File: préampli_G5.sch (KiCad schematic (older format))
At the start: 44 parts, among them J1 Input, J2 Barrel_Jack, J3 Output, SW1 Boost, U1 ECC83, U2 ECC83, U3 NCH6100HV

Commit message: Use a self-split PP for the output stage
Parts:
- removed C10: 10µF, symbol Device:CP
- removed C8: 470pF, symbol Device:C
- removed R13: 470k, symbol Device:R
- removed R15: 100k, symbol Device:R
- removed R17: 10k, symbol Device:R
- added R6: 220k, symbol Device:R
- added TR1: HAMMOND 125A, symbol Transformer:TRANSF4
- R14: value 1.8k -> 1k
- R16: value 91k -> 180R/2W
- U3: symbol Converter_DCDC:NCH6100HV -> préampli_G5-rescue:NCH6100HV-Converter_DCDC
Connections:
- net GND: now also R16.2, SW1.4, U2.7 (G), TR1.4
- net GNDPWR: now also U3.2 (SHDN)
- net at C6.1, R20.1, R8.1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: no longer SW1.3
- net at R11.2, R12.1, R19.1: now also R6.1
- net at U2.1 (A): now also TR1.1; no longer U2.7 (G)
- net at U2.2 (G): now also R6.2
- net at R14.1, U2.3 (K): now also U2.8 (K)
- net at C9.1, R10.1, R18.2: now also TR1.2; no longer U2.6 (A)
- net at R16.1: now also RV6.3, TR1.5; no longer U2.8 (K)
- net at R19.2: now also SW1.3; no longer SW1.4
- new net: TR1.3, U2.6 (A)
- no-connect marks 1 -> 0
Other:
- note added: "NOTE: TR1 OUPUT ON PINS 3 & 5\nVOLTAGE RATIO 46.9:1 (-33.4 dB)\nIMPEDANCE RATIO 2200:1\nPRIMARY IMPEDANCE 336kΩ (168kΩ PER ANODE)"
- moved on the sheet: C11, J3, R14, R19, R20, RV6, SW1

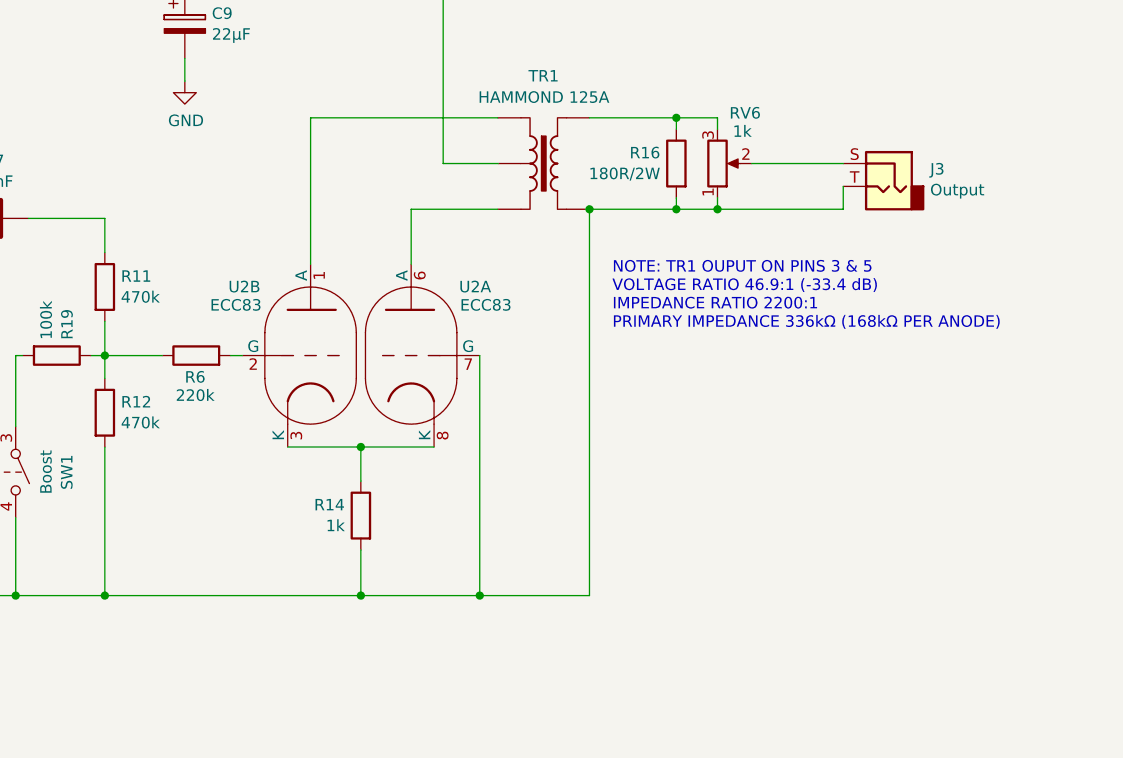
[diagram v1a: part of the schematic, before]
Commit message: Switch to LTP & fix transformer load
180R value for R16 wasn't appropriate, as we should aim for a 100k anode
load for the output stage. Replacing it with 100R will give us the right
primary impedance.

Also, the self-split output stage seems to be quite unbalanced,
switching back to an LTP circuit will improve things.
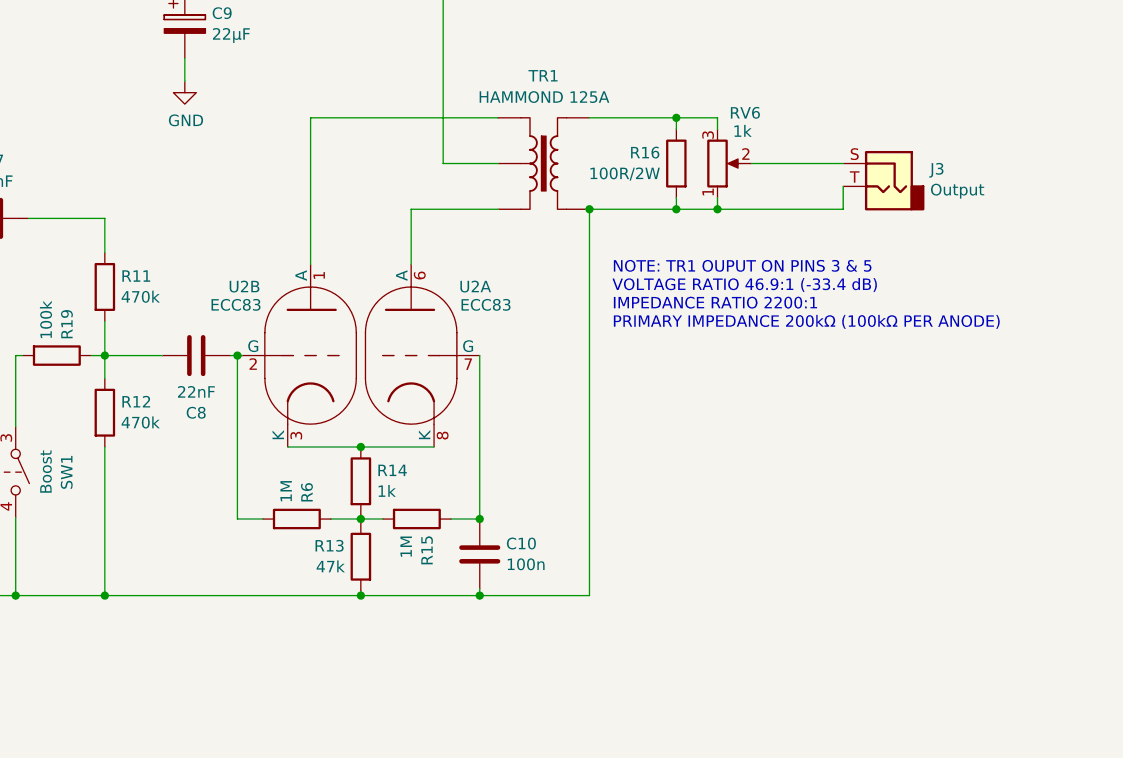
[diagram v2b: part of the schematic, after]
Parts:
- added C10: 100n, symbol Device:C
- added C8: 22nF, symbol Device:C
- added R13: 47k, symbol Device:R
- added R15: 1M, symbol Device:R
- R16: value 180R/2W -> 100R/2W
- R6: value 220k -> 1M
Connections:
- net GND: now also C10.2, R13.2; no longer R14.2, U2.7 (G)
- net at R11.2, R12.1, R19.1: now also C8.2; no longer R6.1
- net at R6.2, U2.2 (G): now also C8.1
- new net: R13.1, R14.2, R15.2, R6.1
- new net: C10.1, R15.1, U2.7 (G)
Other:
- note added: "NOTE: TR1 OUPUT ON PINS 3 & 5\nVOLTAGE RATIO 46.9:1 (-33.4 dB)\nIMPEDANCE RATIO 2200:1\nPRIMARY IMPEDANCE 200kΩ (100kΩ PER ANODE)"
- note removed: "NOTE: TR1 OUPUT ON PINS 3 & 5\nVOLTAGE RATIO 46.9:1 (-33.4 dB)\nIMPEDANCE RATIO 2200:1\nPRIMARY IMPEDANCE 336kΩ (168kΩ PER ANODE)"
- moved on the sheet: R14
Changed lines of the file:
@@
 L Device:R R14
 U 1 1 5C6DBFC3
-P 7820 3800
-F 0 "R14" H 7890 3846 50  0000 L CNN
-F 1 "1k" H 7890 3755 50  0000 L CNN
-F 2 "" V 7750 3800 50  0001 C CNN
-F 3 "~" H 7820 3800 50  0001 C CNN
-	1    7820 3800
-	-1   0    0    -1
+P 7820 3650
+F 0 "R14" H 7890 3696 50  0000 L CNN
+F 1 "1k" H 7890 3605 50  0000 L CNN
+F 2 "" V 7750 3650 50  0001 C CNN
+F 3 "~" H 7820 3650 50  0001 C CNN
+	1    7820 3650
+	1    0    0    -1
 $EndComp
 $Comp
@@
 	6700 2950 6700 3100
 Wire Wire Line
-	7300 3100 7250 3100
+	7300 3100 7280 3100
 Connection ~ 6700 3100
 Wire Wire Line
@@
 P 9200 2260
 F 0 "R16" H 9270 2306 50  0000 L CNN
-F 1 "180R/2W" H 9270 2215 50  0000 L CNN
+F 1 "100R/2W" H 9270 2215 50  0000 L CNN
 F 2 "" V 9130 2260 50  0001 C CNN
 F 3 "~" H 9200 2260 50  0001 C CNN
@@
 	8820 2060 9200 2060
 Text Notes 8920 2990 0    50   ~ 0
-NOTE: TR1 OUPUT ON PINS 3 & 5\nVOLTAGE RATIO 46.9:1 (-33.4 dB)\nIMPEDANCE RATIO 2200:1\nPRIMARY IMPEDANCE 336kΩ (168kΩ PER ANODE)
+NOTE: TR1 OUPUT ON PINS 3 & 5\nVOLTAGE RATIO 46.9:1 (-33.4 dB)\nIMPEDANCE RATIO 2200:1\nPRIMARY IMPEDANCE 200kΩ (100kΩ PER ANODE)
 Wire Wire Line
 	8820 4150 8820 2460
 Connection ~ 8820 2460
 Wire Wire Line
+	8340 3100 8340 3815
+Connection ~ 8340 4150
+Wire Wire Line
+	8340 4150 8820 4150
+Wire Wire Line
+	7500 3500 7820 3500
+Wire Wire Line
 	6700 4150 7820 4150
-Wire Wire Line
-	7500 3500 7820 3500
-Wire Wire Line
-	7820 3650 7820 3500
 Connection ~ 7820 3500
 Wire Wire Line
 	7820 3500 8140 3500
-Wire Wire Line
-	7820 3950 7820 4150
-Connection ~ 7820 4150
-Wire Wire Line
-	7820 4150 8340 4150
-Wire Wire Line
-	8340 3100 8340 4150
-Connection ~ 8340 4150
-Wire Wire Line
-	8340 4150 8820 4150
+$Comp
+L Device:R R13
+U 1 1 5C7859F7
+P 7820 3980
+F 0 "R13" H 7890 4026 50  0000 L CNN
+F 1 "47k" H 7890 3935 50  0000 L CNN
+F 2 "" V 7750 3980 50  0001 C CNN
+F 3 "~" H 7820 3980 50  0001 C CNN
+	1    7820 3980
+	-1   0    0    -1
+$EndComp
+$Comp
+L Device:R R15
+U 1 1 5C785AB9
+P 8065 3815
+F 0 "R15" H 8135 3861 50  0000 L CNN
+F 1 "1M" H 8135 3770 50  0000 L CNN
+F 2 "" V 7995 3815 50  0001 C CNN
+F 3 "~" H 8065 3815 50  0001 C CNN
+	1    8065 3815
+	0    1    1    0
+$EndComp
 $Comp
 L Device:R R6
-U 1 1 5C87E139
+U 1 1 5C785C4B
+P 7540 3815
+F 0 "R6" H 7610 3861 50  0000 L CNN
+F 1 "1M" H 7610 3770 50  0000 L CNN
+F 2 "" V 7470 3815 50  0001 C CNN
+F 3 "~" H 7540 3815 50  0001 C CNN
+	1    7540 3815
+	0    1    -1   0
+$EndComp
+$Comp
+L Device:C C8
+U 1 1 5C78E544
 P 7100 3100
-F 0 "R6" V 7005 3105 50  0000 C CNN
-F 1 "220k" V 6925 3105 50  0000 C CNN
-F 2 "" V 7030 3100 50  0001 C CNN
+F 0 "C8" V 6848 3100 50  0000 C CNN
+F 1 "22nF" V 6939 3100 50  0000 C CNN
+F 2 "" H 7138 2950 50  0001 C CNN
 F 3 "~" H 7100 3100 50  0001 C CNN
 	1    7100 3100
-	0    -1   -1   0
-$EndComp
+	0    1    -1   0
+$EndComp
+Wire Wire Line
+	7280 3100 7280 3815
+Wire Wire Line
+	7280 3815 7390 3815
+Connection ~ 7280 3100
+Wire Wire Line
+	7280 3100 7250 3100
+Wire Wire Line
+	7690 3815 7820 3815
+Wire Wire Line
+	7820 3800 7820 3815
+Connection ~ 7820 3815
+Wire Wire Line
+	7820 3815 7915 3815
+Wire Wire Line
+	7820 3815 7820 3830
+Wire Wire Line
+	7820 4130 7820 4150
+Connection ~ 7820 4150
+Wire Wire Line
+	7820 4150 8340 4150
+$Comp
+L Device:C C10
+U 1 1 5C7A8FB8
+P 8340 3970
+F 0 "C10" H 8455 4016 50  0000 L CNN
+F 1 "100n" H 8455 3925 50  0000 L CNN
+F 2 "" H 8378 3820 50  0001 C CNN
+F 3 "~" H 8340 3970 50  0001 C CNN
+	1    8340 3970
+	1    0    0    -1
+$EndComp
+Wire Wire Line
+	8340 4120 8340 4150
+Wire Wire Line
+	8215 3815 8340 3815
+Connection ~ 8340 3815
+Wire Wire Line
+	8340 3815 8340 3820
 $EndSCHEMATC
